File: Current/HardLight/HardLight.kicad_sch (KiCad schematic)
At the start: 45 parts, among them J0 USB, J1 qwiic, U0 RP2040, U1 LDO-3.3, U2 USBLC6-2SC6, U3 W25Q128JVS, Y0 12MHz

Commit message: HL Mark 7 primary update
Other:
- removed sheet Matrix
- added sheet User Interface Element (HardLight-Matrix.kicad_sch)

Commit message: eat shit and die
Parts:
- added J2: MicroCon, EDI:MicroCon-2, symbol Connector:Conn_01x02_Female
- added J3: MicroCon, EDI:MicroCon-3, symbol Connector:Conn_01x03_Female
- F0: footprint Fuse:Fuse_0603_1608Metric_Castellated -> Fuse:Fuse_0603_1608Metric
- J1: symbol Connector_Generic:Conn_01x04 -> Connector_Generic:Conn_01x05
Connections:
- net 13: now also J3.3 (Pin_3)
- net 14: now also J3.2 (Pin_2)
- net 15: now also J3.1 (Pin_1)
- net 21: now also J2.1 (Pin_1)
- net 22: now also J2.2 (Pin_2)
- net GND: now also J1.MP
- no-connect marks 9 -> 4

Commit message: get brent
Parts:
- S1, S2: LCSC C140848 -> C139779
- Y0: value 12MHz -> 2TJ412000NYGBC 12MHz
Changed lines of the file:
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@@
   (title_block
     (title "Hard Light")
-    (date "2021-10-26")
-    (rev "2040 Mark 1")
+    (date "2022-05-20")
+    (rev "Mark 7")
     (company "Everywhere Defense Industries")
     (comment 1 "RP2040 main core")
@@
     (in_bom yes) (on_board yes)
     (property "Reference" "J1" (id 0) (at 132.08 137.795 0))
-    (property "Value" "qwiic" (id 1) (at 134.62 131.445 90))
+    (property "Value" "qwiic" (id 1) (at 128.27 130.175 90))
     (property "Footprint" "Connector_JST:JST_SH_SM04B-SRSS-TB_1x04-1MP_P1.00mm_Horizontal" (id 2) (at 132.08 130.175 0)
       (effects (font (size 1.27 1.27)) hide)
@@
   (symbol (lib_id "Device:C_Small") (at 169.545 36.83 180) (unit 1)
     (in_bom yes) (on_board yes)
-    (property "Reference" "CP0" (id 0) (at 167.2082 37.9984 0)
+    (property "Reference" "CP0" (id 0) (at 167.005 38.1 0)
       (effects (font (size 1.27 1.27)) (justify left))
     )
-    (property "Value" "1uf" (id 1) (at 167.2082 35.687 0)
+    (property "Value" "1uf" (id 1) (at 167.005 35.56 0)
       (effects (font (size 1.27 1.27)) (justify left))
     )
@@
     (in_bom yes) (on_board yes)
     (property "Reference" "Y0" (id 0) (at 90.17 128.905 90))
-    (property "Value" "12MHz" (id 1) (at 80.01 128.905 90))
+    (property "Value" "2TJ412000NYGBC 12MHz" (id 1) (at 80.01 128.905 0))
     (property "Footprint" "Crystal:Crystal_SMD_2520-4Pin_2.5x2.0mm" (id 2) (at 90.17 128.905 0)
       (effects (font (size 1.27 1.27)) hide)
@@
       (effects (font (size 1.27 1.27)) hide)
     )
-    (property "LCSC" "C140848" (id 4) (at 177.165 58.42 0)
+    (property "LCSC" "C139779" (id 4) (at 177.165 58.42 0)
       (effects (font (size 1.27 1.27)) hide)
     )
@@
       (effects (font (size 1.27 1.27)) hide)
     )
-    (property "LCSC" "C140848" (id 4) (at 213.995 33.655 0)
+    (property "LCSC" "C139779" (id 4) (at 213.995 33.655 0)
       (effects (font (size 1.27 1.27)) hide)
     )
@@
   (symbol (lib_id "Device:C_Small") (at 184.785 36.83 0) (unit 1)
     (in_bom yes) (on_board yes)
-    (property "Reference" "CP1" (id 0) (at 187.1218 35.6616 0)
+    (property "Reference" "CP1" (id 0) (at 187.325 38.1 0)
       (effects (font (size 1.27 1.27)) (justify left))
     )
-    (property "Value" "1uf" (id 1) (at 187.1218 37.973 0)
+    (property "Value" "1uf" (id 1) (at 187.325 35.56 0)
       (effects (font (size 1.27 1.27)) (justify left))
     )
@@
     )
     (path "/46b6fcd5-0947-44f0-ab4d-0e5313e0c1b9"
-      (reference "Y0") (unit 1) (value "12MHz") (footprint "Crystal:Crystal_SMD_2520-4Pin_2.5x2.0mm")
+      (reference "Y0") (unit 1) (value "2TJ412000NYGBC 12MHz") (footprint "Crystal:Crystal_SMD_2520-4Pin_2.5x2.0mm")
     )
     (path "/00000000-0000-0000-0000-000061ea0765"

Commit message: yep it's good now
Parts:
- H1, H2, H3, H4, H5, H6, H7, H8: footprint MountingHole:MountingHole_2.2mm_M2_ISO7380_Pad -> MountingHole:MountingHole_3.2mm_M3; symbol Mechanical:MountingHole_Pad -> Mechanical:MountingHole
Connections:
- net GND: no longer H1.1, H2.1, H3.1, H4.1, H5.1, H6.1, H7.1, H8.1

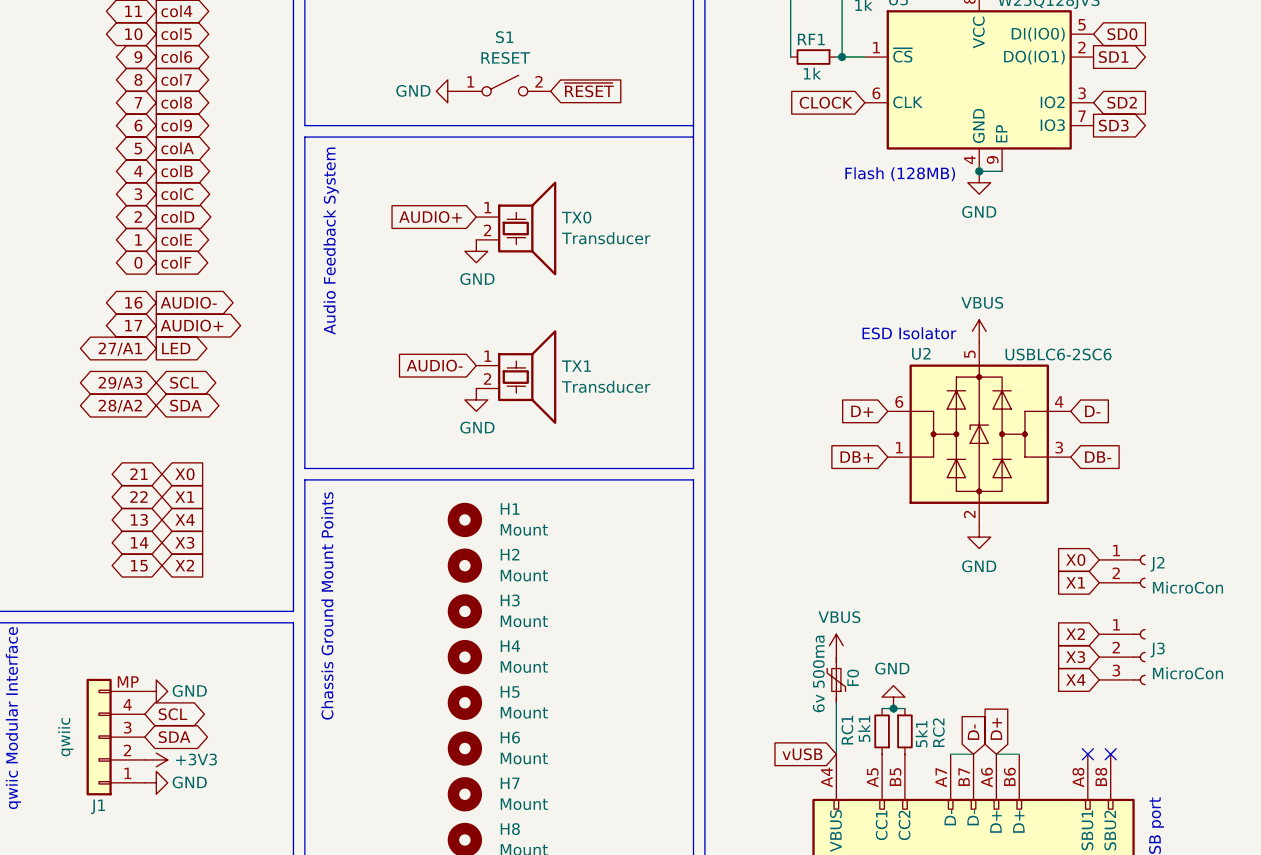
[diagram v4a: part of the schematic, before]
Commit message: Yep, moved some stuff to archives.
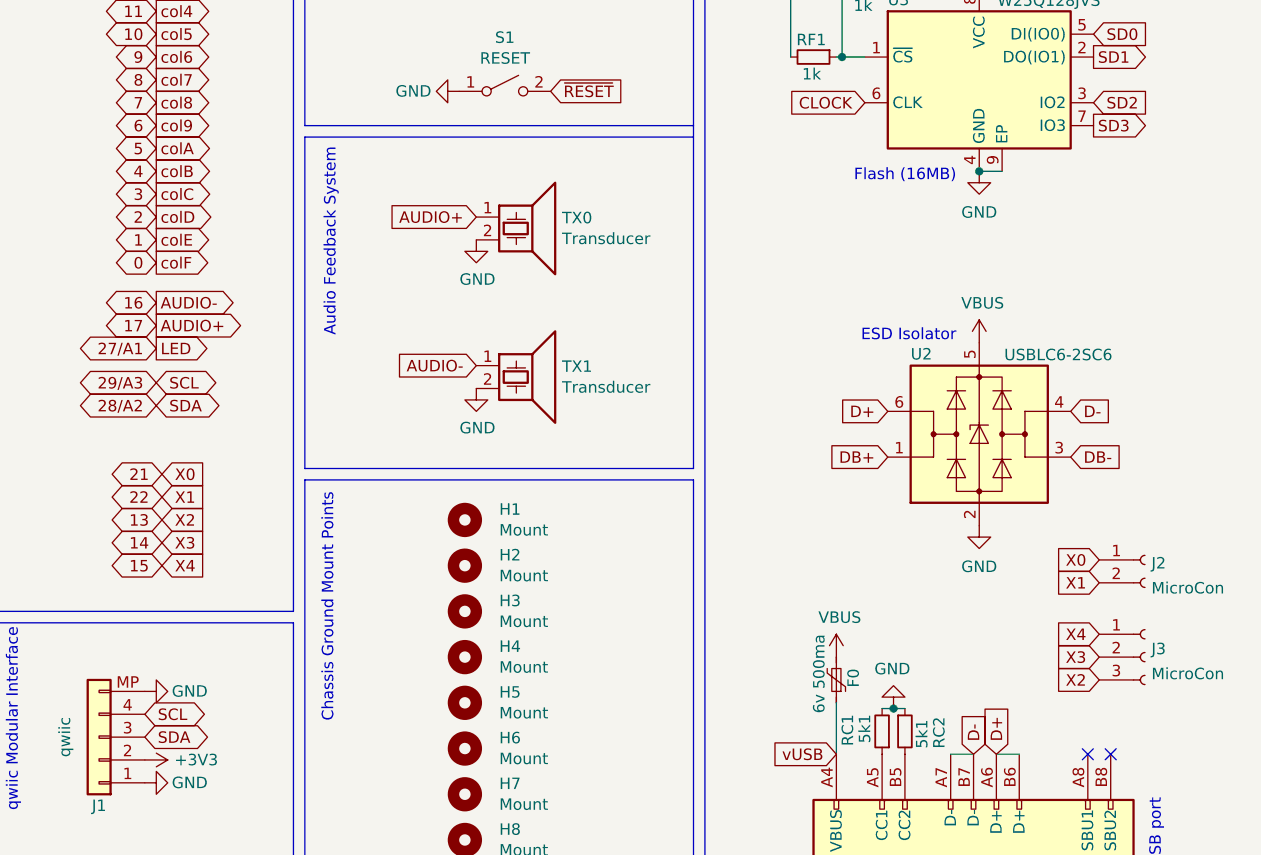
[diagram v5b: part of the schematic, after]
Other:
- note added: "Flash (16MB)"
- note removed: "Flash (128MB)"

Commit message: So much stuff
Wow it's been a while.
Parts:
- removed CX1, CX2: 13pf, EDI:Passive_0402_1005Metric, symbol Device:C_Small
- removed J2: MicroCon, EDI:MicroCon-2, symbol Connector:Conn_01x02_Female
- removed J3: MicroCon, EDI:MicroCon-3, symbol Connector:Conn_01x03_Female
- removed RF1: 1k, EDI:Passive_0402_1005Metric, symbol Device:R_Small
- removed S2: USB BOOT, Button_Switch_SMD:SW_SPST_SKQG_WithoutStem, symbol Switch:SW_SPST
- removed Y0: 2TJ412000NYGBC 12MHz, Crystal:Crystal_SMD_2520-4Pin_2.5x2.0mm, symbol Device:Crystal_GND24
- added J2: SPI Connector, Connector_JST:JST_SH_SM06B-SRSS-TB_1x06-1MP_P1.00mm_Horizontal, symbol Connector:Conn_01x07_Female
- added TP0: 22, TestPoint:TestPoint_Pad_1.0x1.0mm, symbol Connector:TestPoint
- added Y0: CSTCE12M0G55-R0, Crystal:Resonator_SMD_Murata_CSTxExxV-3Pin_3.0x1.1mm, symbol Device:Crystal_GND2_Small
- F0: footprint Fuse:Fuse_0603_1608Metric -> Fuse:Fuse_0402_1005Metric; LCSC C207011 -> C206938
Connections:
- net +3V3: now also J2.1 (Pin_1)
- net 18: now also J2.5 (Pin_5)
- net 19: now also J2.4 (Pin_4)
- net 20: now also J2.3 (Pin_3)
- net 21: now also J2.2 (Pin_2)
- net 22: now also TP0.1
- net GND: now also J2.6 (Pin_6), J2.MP, Y0.2
- net XIN: now also Y0.1
- net XOUT1: no longer names the net of RX1.2
- net XOUT1: now also Y0.3
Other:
- moved on the sheet: CF1, F0, J0, RC1, RC2, RF2, U2, U3
